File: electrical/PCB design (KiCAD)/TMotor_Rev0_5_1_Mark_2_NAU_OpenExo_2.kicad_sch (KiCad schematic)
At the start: 34 parts, among them J10 XT30PW-F, J11 XT30PW-F, J2 Conn_01x04_Pin, J3 Conn_01x02_Pin, J4 Conn_01x02_Pin, J5 Conn_01x02_Pin, J6 Conn_01x03_Pin, J7 XT30PW-F, J8 XT30PW-F, J9 XT30PW-F, U8 SN65HVD230DR, U9 WPME-FDSM_SIP-3

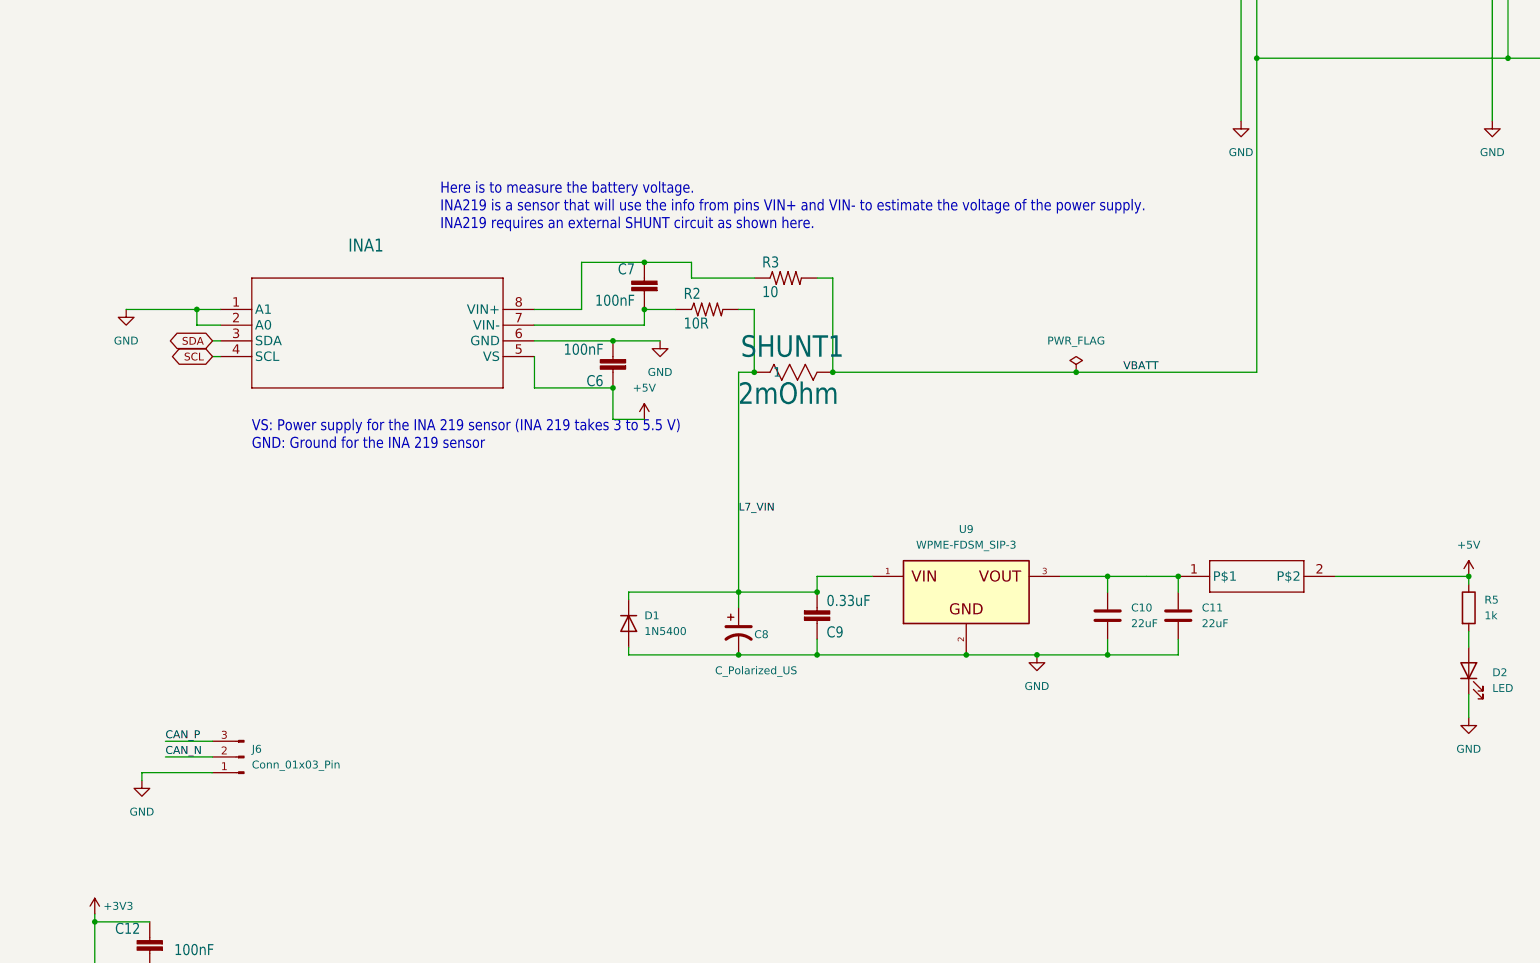
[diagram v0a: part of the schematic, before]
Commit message: fix modularize python script for ble.py and sensors.py (main and plotting-csv not done
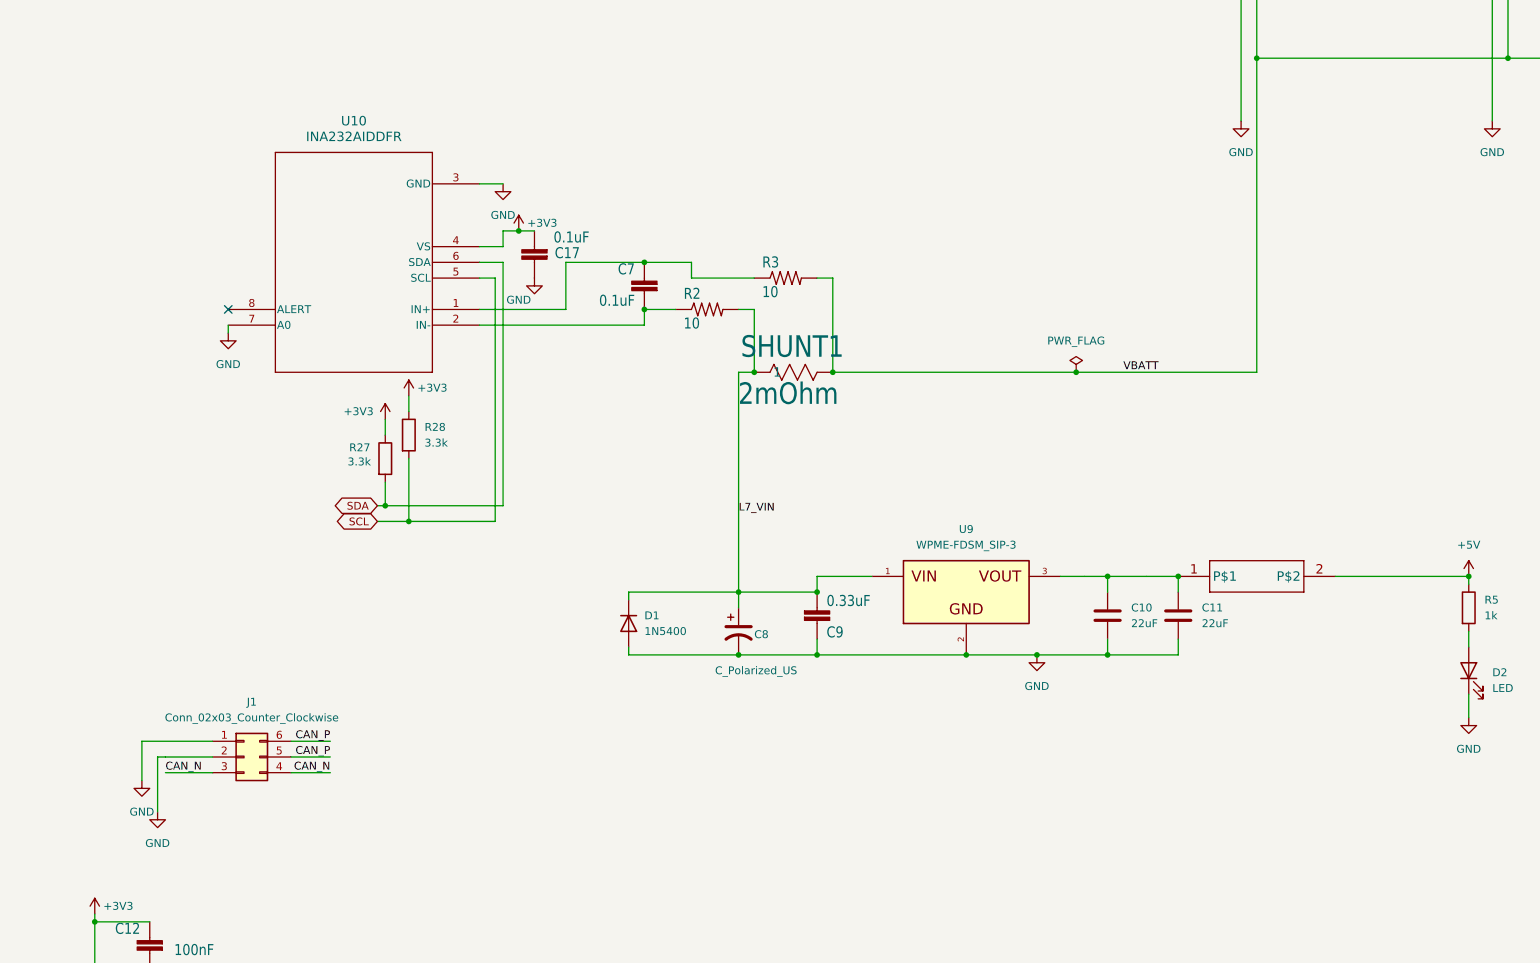
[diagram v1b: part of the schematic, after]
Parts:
- removed C6: 100nF, Capacitor_SMD:C_0805_2012Metric_Pad1.18x1.45mm_HandSolder, symbol TMotor_Rev0_5_1_Mark_2_NAU_OpenExo-eagle-import:C-EU050-024X044
- removed INA1: ~, TMotor_Rev0_5_1_Mark_2_NAU_OpenExo:D8_TEX, symbol TMotor_Rev0_5_1_Mark_2_NAU_OpenExo-eagle-import:INA219AIDR
- removed J6: Conn_01x03_Pin, Connector_PinHeader_2.54mm:PinHeader_1x03_P2.54mm_Vertical, symbol Connector:Conn_01x03_Pin
- added C17: 0.1uF, Capacitor_SMD:C_0805_2012Metric_Pad1.18x1.45mm_HandSolder, symbol TMotor_Rev0_5_1_Mark_2_NAU_OpenExo-eagle-import:C-EU050-024X044
- added J1: Conn_02x03_Counter_Clockwise, Connector_PinHeader_2.54mm:PinHeader_2x03_P2.54mm_Vertical, symbol Connector_Generic:Conn_02x03_Counter_Clockwise
- added R27, R28: 3.3k, Resistor_SMD:R_0805_2012Metric_Pad1.20x1.40mm_HandSolder, symbol Device:R
- added U10: INA232AIDDFR, SOT_32AIDDFR_TEX, symbol INA232AIDDFR:INA232AIDDFR
- C7: value 100nF -> 0.1uF
- R2: value 10R -> 10
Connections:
- net +3V3: now also C17.2, R27.1, R28.1, U10.4 (VS)
- net CAN_N: now also J1.3 (Pin_3), J1.4 (Pin_4)
- net CAN_P: now also J1.5 (Pin_5), J1.6 (Pin_6)
- net GND: now also C17.1, J1.1 (Pin_1), J1.2 (Pin_2), U10.3 (GND), U10.7 (A0)
- net SCL: now also R28.2, U10.5 (SCL)
- net SDA: now also R27.2, U10.6 (SDA)
- net at C7.2, R2.1: now also U10.2 (IN-)
- net at C7.1, R3.1: now also U10.1 (IN+)
- no-connect marks 1 -> 2
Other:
- note removed: "Here is to measure the battery voltage. INA219 is a sensor that will use the info from pins VIN+ and VIN- to estimate the voltage of the power supply. INA219 requires an external SHUNT circuit as shown here."
- note removed: "VS: Power supply for the INA 219 sensor (INA 219 takes 3 to 5.5 V) GND: Ground for the INA 219 sensor"
